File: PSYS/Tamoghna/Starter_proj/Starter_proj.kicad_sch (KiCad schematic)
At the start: 41 parts, among them J1 Conn_Coaxial, J2 Conn_ARM_SWD_TagConnect_TC2030, J3 USB_C_Receptacle_USB2.0_16P, J4 Conn_01x04, SW1 SW_Push, U1 STM32WB55CEUx, U2 USBLC6-2SC6, U3 MIC5365-3.3YD5, Y1 32Mhz, Y2 32kHz768

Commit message: footprints assigned
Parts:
- removed Y1: 32Mhz, symbol Device:Crystal
- added Y1: Crystal_GND24, Crystal:Crystal_SMD_2016-4Pin_2.0x1.6mm, symbol Device:Crystal_GND24
- C1, C15, C16, C17, C2, C3, C4, C5, C6: footprint (none) -> Capacitor_SMD:C_0603_1608Metric
- C10, C11, C12, C13, C14, C7, C8, C9: footprint (none) -> Capacitor_SMD:C_0402_1005Metric
- C18, C19: footprint Package_TO_SOT_SMD:TSOT-23-5 -> Capacitor_SMD:C_0603_1608Metric
- D1: footprint (none) -> LED_SMD:LED_0603_1608Metric
- J1: footprint (none) -> Connector_Coaxial:U.FL_Hirose_U.FL-R-SMT-1_Vertical
- J3: footprint (none) -> Connector_USB:USB_C_Receptacle_GCT_USB4105-xx-A_16P_TopMnt_Horizontal
- J4: footprint (none) -> Connector_PinHeader_2.54mm:PinHeader_1x04_P2.54mm_Vertical
- L1: footprint (none) -> Inductor_SMD:L_0402_1005Metric
- L2: footprint (none) -> Inductor_SMD:L_0805_2012Metric
- L3: value L -> 2n7; footprint Package_SO:SOIC-16_3.9x9.9mm_P1.27mm -> Inductor_SMD:L_0402_1005Metric
- R1, R2, R3, R4, R5, R6, R7: footprint (none) -> Resistor_SMD:R_0603_1608Metric
- Y2: footprint (none) -> Crystal:Crystal_SMD_3215-2Pin_3.2x1.5mm
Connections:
- net HSE_IN: now also Y1.1
- net HSE_OUT: now also Y1.3
- net smplx renamed SMPLX
- new net: Y1.2 (G), Y1.4 (G)
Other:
- moved on the sheet: J2

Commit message: math added
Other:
- note added: "(3.3V - 2.0V) / 0.006A"
- note added: "0.00051s / 5.1koh"
- note added: "2 * (7pF - 2pF)"
- note added: "3.3V / 0.015A"
- note added: "3.3V / 0.647A"
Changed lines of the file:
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@@
 		(company "LHR Solar")
+	)
+	(text " 3.3V / 0.647A"
+		(exclude_from_sim no)
+		(at 206.248 105.918 90)
+		(effects
+			(font
+				(size 0.762 0.762)
+			)
+		)
 	)
 	(text "+5v to +3v3 LDO Regulator\n"
@@
 			(font
 				(size 1.27 1.27)
+			)
+		)
+	)
+	(text " 3.3V / 0.015A"
+		(exclude_from_sim no)
+		(at 219.456 95.25 0)
+		(effects
+			(font
+				(size 0.762 0.762)
+			)
+		)
+	)
+	(text "0.00051s / 5.1koh"
+		(exclude_from_sim no)
+		(at 221.234 107.696 0)
+		(effects
+			(font
+				(size 0.762 0.762)
 			)
 		)
@@
 		)
 	)
+	(text "3.3V / 0.015A"
+		(exclude_from_sim no)
+		(at 101.346 57.404 0)
+		(effects
+			(font
+				(size 0.762 0.762)
+			)
+		)
+	)
+	(text "2 * (7pF - 2pF)"
+		(exclude_from_sim no)
+		(at 182.372 99.822 0)
+		(effects
+			(font
+				(size 0.762 0.762)
+			)
+		)
+	)
 	(text "RF & u.FL Connector\n"
 		(exclude_from_sim no)
@@
 			)
 		)
+	)
+	(text "(3.3V - 2.0V) / 0.006A"
+		(exclude_from_sim no)
+		(at 96.266 65.532 0)
+		(effects
+			(font
+				(size 0.762 0.762)
+			)
+		)

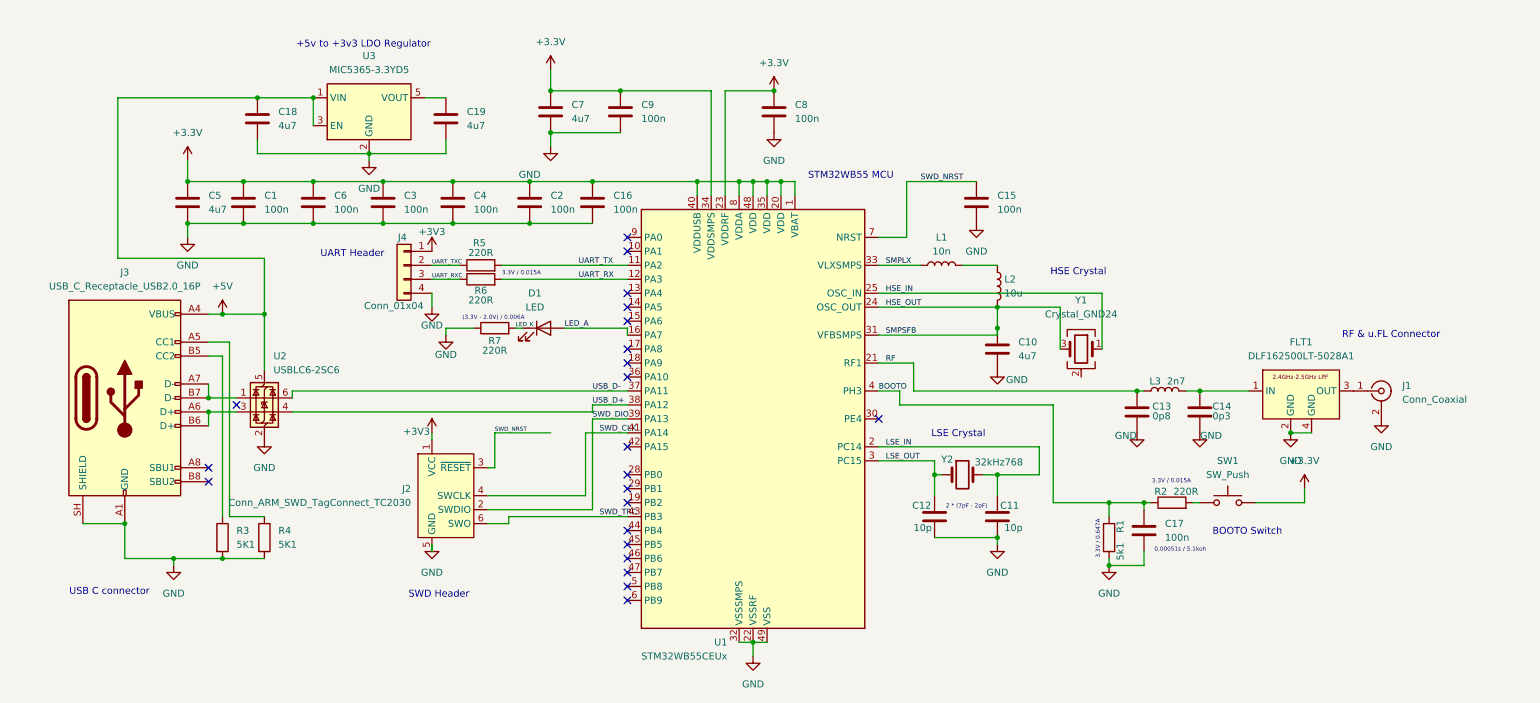
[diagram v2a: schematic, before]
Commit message: pcb layout board setup
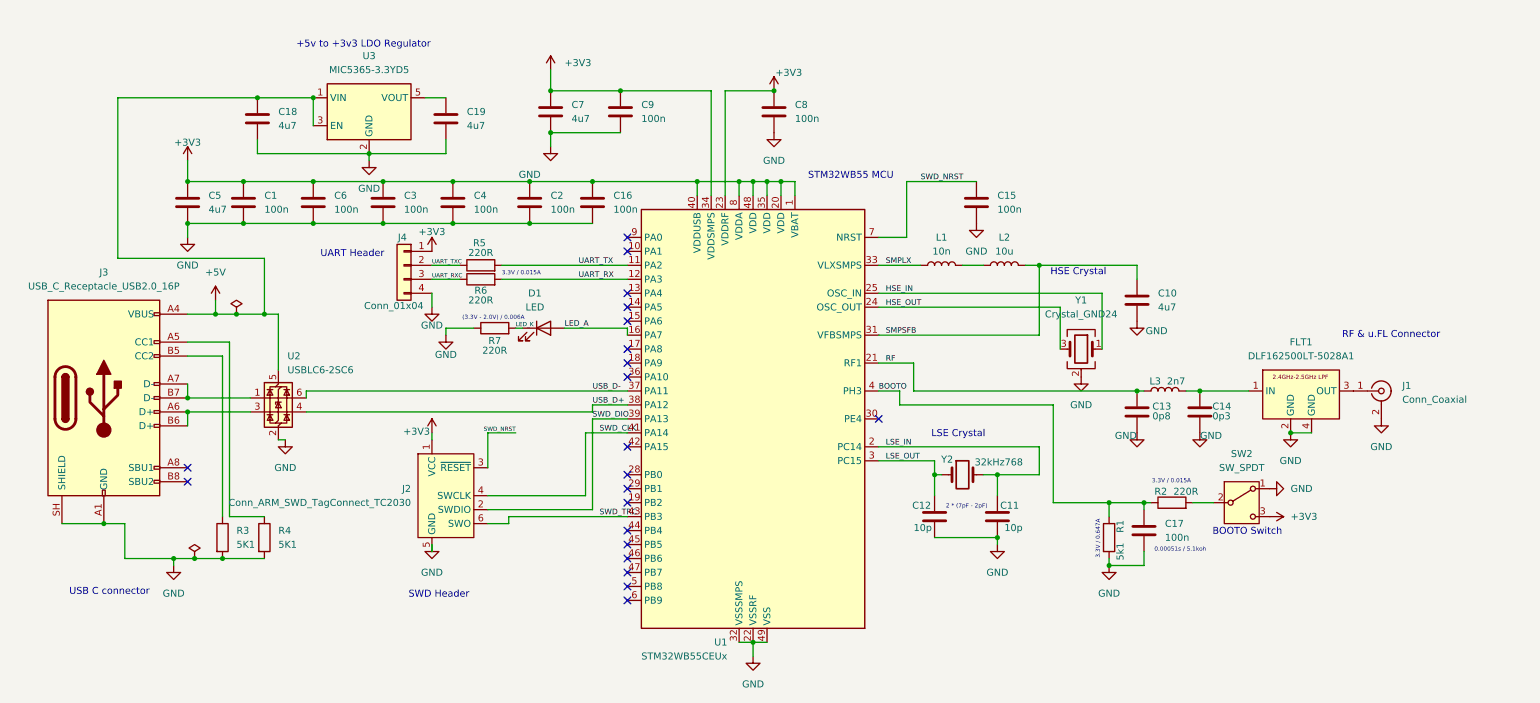
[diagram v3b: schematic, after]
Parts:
- removed SW1: SW_Push, Button_Switch_THT:SW_NKK_GW12LJP, symbol Switch:SW_Push
- added SW2: SW_SPDT, footprintlib:SW_Wurth_WS-SLSV_450406020024, symbol Switch:SW_SPDT
- C10, C7: footprint Capacitor_SMD:C_0402_1005Metric -> Capacitor_SMD:C_0805_2012Metric
- C18, C19, C5: footprint Capacitor_SMD:C_0603_1608Metric -> Capacitor_SMD:C_0805_2012Metric
- C8, C9: footprint Capacitor_SMD:C_0402_1005Metric -> Capacitor_SMD:C_0603_1608Metric
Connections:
- net +3.3V is gone; now on net +3V3: C1.1, C16.1, C2.1, C3.1, C4.1, C5.1, C6.1, C7.1, C8.1, C9.1, U1.1 (VBAT), U1.20 (VDD), U1.23 (VDDRF), U1.34 (VDDSMPS), U1.35 (VDD), U1.40 (VDDUSB), U1.48 (VDD), U1.8 (VDDA)
- net +3V3: now also SW2.3 (C)
- net GND: now also Y1.2 (G), Y1.4 (G), SW2.1 (A)
- net HSE_OUT: no longer C10.1, L2.2, U1.31 (VFBSMPS)
- net at R2.2: now also SW2.2 (B)
- new net SMPSFB: C10.1, L2.2, U1.31 (VFBSMPS)
- no-connect marks 22 -> 21
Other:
- moved on the sheet: C10, J3, L2, U2

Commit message: AHHHHHHHH ALL MY NETS WERE FUCKED FIXED IT
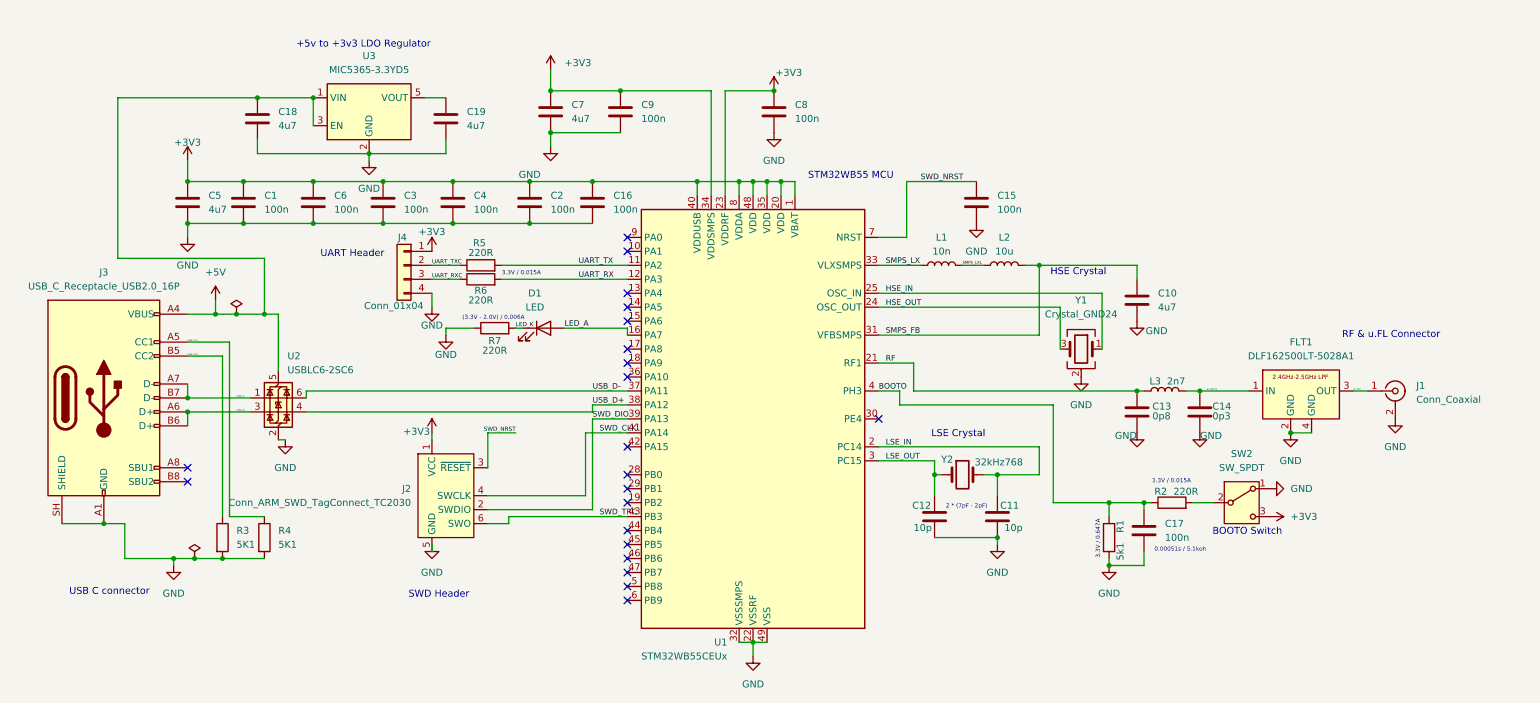
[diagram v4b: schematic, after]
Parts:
- J4: footprint Connector_PinHeader_2.54mm:PinHeader_1x04_P2.54mm_Vertical -> Connector_Molex:Molex_PicoBlade_53047-0410_1x04_P1.25mm_Vertical
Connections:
- net USBC_CC2: now reaches J3.B5 (CC2), R3.1
- net SMPS_LXL: now reaches L1.2, L2.1
- net USBC_CC1: now reaches J3.A5 (CC1), R4.1
- net RF_MATCH: now reaches C14.1, FLT1.1 (IN), L3.2
- net RF_ANT: now reaches FLT1.3 (OUT), J1.1 (In)
- net USBC_D+: now reaches J3.A6 (D+), J3.B6 (D+), U2.3 (I/O2)
- net USBC_D-: now reaches J3.A7 (D-), J3.B7 (D-), U2.1 (I/O1)
- net SMPLX renamed SMPS_LX
- net SMPSFB renamed SMPS_FB
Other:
- moved on the sheet: J1
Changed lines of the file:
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@@
 	(wire
 		(pts
+			(xy 255.27 78.74) (xy 252.73 78.74)
+		)
+		(stroke
+			(width 0)
+			(type default)
+		)
+	)
+	(wire
+		(pts
 			(xy 195.58 93.98) (xy 187.96 93.98)
 		)
@@
 		)
 	)
-	(label "SMPLX"
+	(label "SMPS_LX"
 		(at 167.64 55.88 0)
 		(effects
@@
 		)
 	)
+	(label "USBC_D+"
+		(at 49.53 82.55 0)
+		(effects
+			(font
+				(size 0.254 0.254)
+			)
+			(justify left bottom)
+		)
+	)
 	(label "HSE_IN"
 		(at 167.64 60.96 0)
@@
 		)
 	)
+	(label "USBC_D-"
+		(at 49.53 80.01 0)
+		(effects
+			(font
+				(size 0.254 0.254)
+			)
+			(justify left bottom)
+		)
+	)
 	(label "HSE_OUT"
 		(at 167.64 63.5 0)
@@
 		)
 	)
-	(label "SMPSFB"
+	(label "SMPS_FB"
 		(at 167.64 68.58 0)
 		(effects
@@
 		)
 	)
+	(label "RF_MATCH"
+		(at 226.06 78.74 0)
+		(effects
+			(font
+				(size 0.254 0.254)
+			)
+			(justify left bottom)
+		)
+	)
 	(label "UART_TX"
 		(at 111.76 55.88 0)
@@
 		)
 	)
+	(label "USBC_CC2"
+		(at 40.64 72.39 0)
+		(effects
+			(font
+				(size 0.254 0.254)
+			)
+			(justify left bottom)
+		)
+	)
 	(label "UART_RX"
 		(at 111.76 58.42 0)
@@
 		)
 	)
+	(label "USBC_CC1"
+		(at 40.64 69.85 0)
+		(effects
+			(font
+				(size 0.254 0.254)
+			)
+			(justify left bottom)
+		)
+	)
 	(label "SWD_TRC"
 		(at 115.57 101.6 0)
@@
 		)
 	)
+	(label "SMPS_LXL"
+		(at 181.61 55.88 0)
+		(effects
+			(font
+				(size 0.508 0.508)
+			)
+			(justify left bottom)
+		)
+	)
 	(label "LED_A"
 		(at 109.22 67.31 0)
@@
 		)
 	)
+	(label "RF_ANT"
+		(at 252.73 78.74 0)
+		(effects
+			(font
+				(size 0.254 0.254)
+			)
+			(justify left bottom)
+		)
+	)
 	(label "UART_RXC"
 		(at 85.09 58.42 0)
@@
 	(symbol
 		(lib_id "Connector:Conn_Coaxial")
-		(at 257.81 78.74 0)
+		(at 260.35 78.74 0)
 		(unit 1)
 		(body_style 1)
@@
 		(fields_autoplaced yes)
 		(property "Reference" "J1"
-			(at 261.62 77.7631 0)
+			(at 264.16 77.7631 0)
 			(show_name no)
 			(do_not_autoplace no)
@@
 		)
 		(property "Value" "Conn_Coaxial"
-			(at 261.62 80.3031 0)
+			(at 264.16 80.3031 0)
 			(show_name no)
 			(do_not_autoplace no)
@@
 		)
 		(property "Footprint" "Connector_Coaxial:U.FL_Hirose_U.FL-R-SMT-1_Vertical"
-			(at 257.81 78.74 0)
+			(at 260.35 78.74 0)
 			(hide yes)
 			(show_name no)
@@
 		)
 		(property "Datasheet" ""
-			(at 257.81 78.74 0)
+			(at 260.35 78.74 0)
 			(hide yes)
 			(show_name no)
@@
 		)
 		(property "Description" "coaxial connector (BNC, SMA, SMB, SMC, Cinch/RCA, LEMO, ...)"
-			(at 257.81 78.74 0)
+			(at 260.35 78.74 0)
 			(hide yes)
 			(show_name no)
@@
 	(symbol
 		(lib_id "power:GND")
-		(at 257.81 83.82 0)
+		(at 260.35 83.82 0)
 		(unit 1)
 		(body_style 1)
@@
 		(fields_autoplaced yes)
 		(property "Reference" "#PWR013"
-			(at 257.81 90.17 0)
+			(at 260.35 90.17 0)
 			(hide yes)
 			(show_name no)
@@
 		)
 		(property "Value" "GND"
-			(at 257.81 88.9 0)
+			(at 260.35 88.9 0)
 			(show_name no)
 			(do_not_autoplace no)
@@
 		)
 		(property "Footprint" "footprintlib:Untitled"
-			(at 257.81 83.82 0)
+			(at 260.35 83.82 0)
 			(hide yes)
 			(show_name no)
@@
 		)
 		(property "Datasheet" ""
-			(at 257.81 83.82 0)
+			(at 260.35 83.82 0)
 			(hide yes)
 			(show_name no)
@@
 		)
 		(property "Description" "Power symbol creates a global label with name \"GND\" , ground"
-			(at 257.81 83.82 0)
+			(at 260.35 83.82 0)
 			(hide yes)
 			(show_name no)
@@
 			)
 		)
-		(property "Footprint" "Connector_PinHeader_2.54mm:PinHeader_1x04_P2.54mm_Vertical"
+		(property "Footprint" "Connector_Molex:Molex_PicoBlade_53047-0410_1x04_P1.25mm_Vertical"
 			(at 80.01 55.88 0)
 			(hide yes)

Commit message: mmm yes i forgot to commit
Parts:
- J2: renamed from J4; value Conn_01x04 -> MOLEX_UART
- renumbered C5 to C1, C16 to C10, C9 to C11, C8 to C12, C12 to C13, C15 to C14, C11 to C15, C10 to C16, C13 to C17, C17 to C18, C14 to C19, C1 to C2, C18 to C3, C6 to C4, C3 to C5, C19 to C6, C4 to C7, C2 to C8, C7 to C9, J3 to J1, J2 to J3, J1 to J4, R3 to R1, R4 to R2, R5 to R3, R6 to R4, R7 to R5, R1 to R6, R2 to R7, SW2 to SW1, U2 to U1, U3 to U2, U1 to U3, Y2 to Y1, Y1 to Y2
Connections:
- net +3V3: now also C6.1, U2.5 (VOUT); no longer U3.23 (VDDRF), U3.34 (VDDSMPS)
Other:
- note added: "Decoupling Caps"
- note added: "VDDRF"
- note added: "VDDSMPS"
- moved on the sheet: C1, C10, C11, C12, C14, C2, C3, C4, C5, C6, C7, C8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
